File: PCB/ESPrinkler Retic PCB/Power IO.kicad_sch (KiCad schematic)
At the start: 23 parts, among them J1 Conn_01x02, J5 Conn_01x02, J6 Conn_01x02, J7 Conn_01x10, Q2 Q_NMOS, Q3 Q_NMOS, U2 LM2596S-5

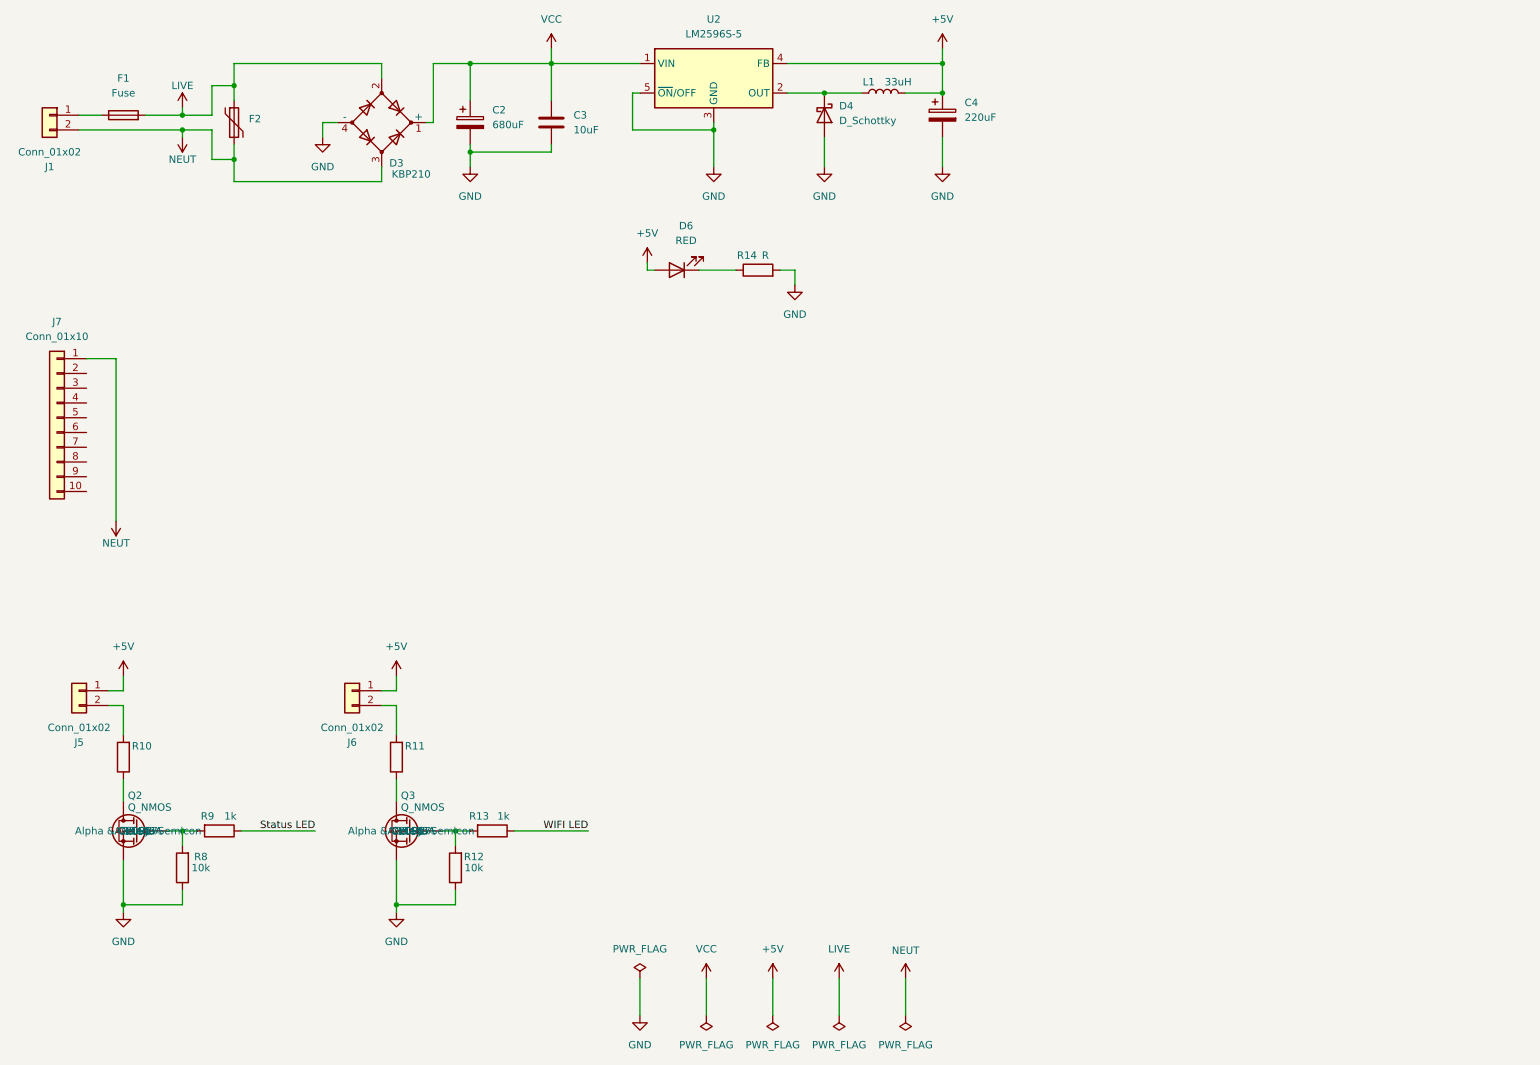
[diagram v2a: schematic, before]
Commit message: Initial schematic design completed
Finish initial schematic design and source all required components. DRC completed with only minor warnings (regarding net names, no worries). Move on to begin PCB design
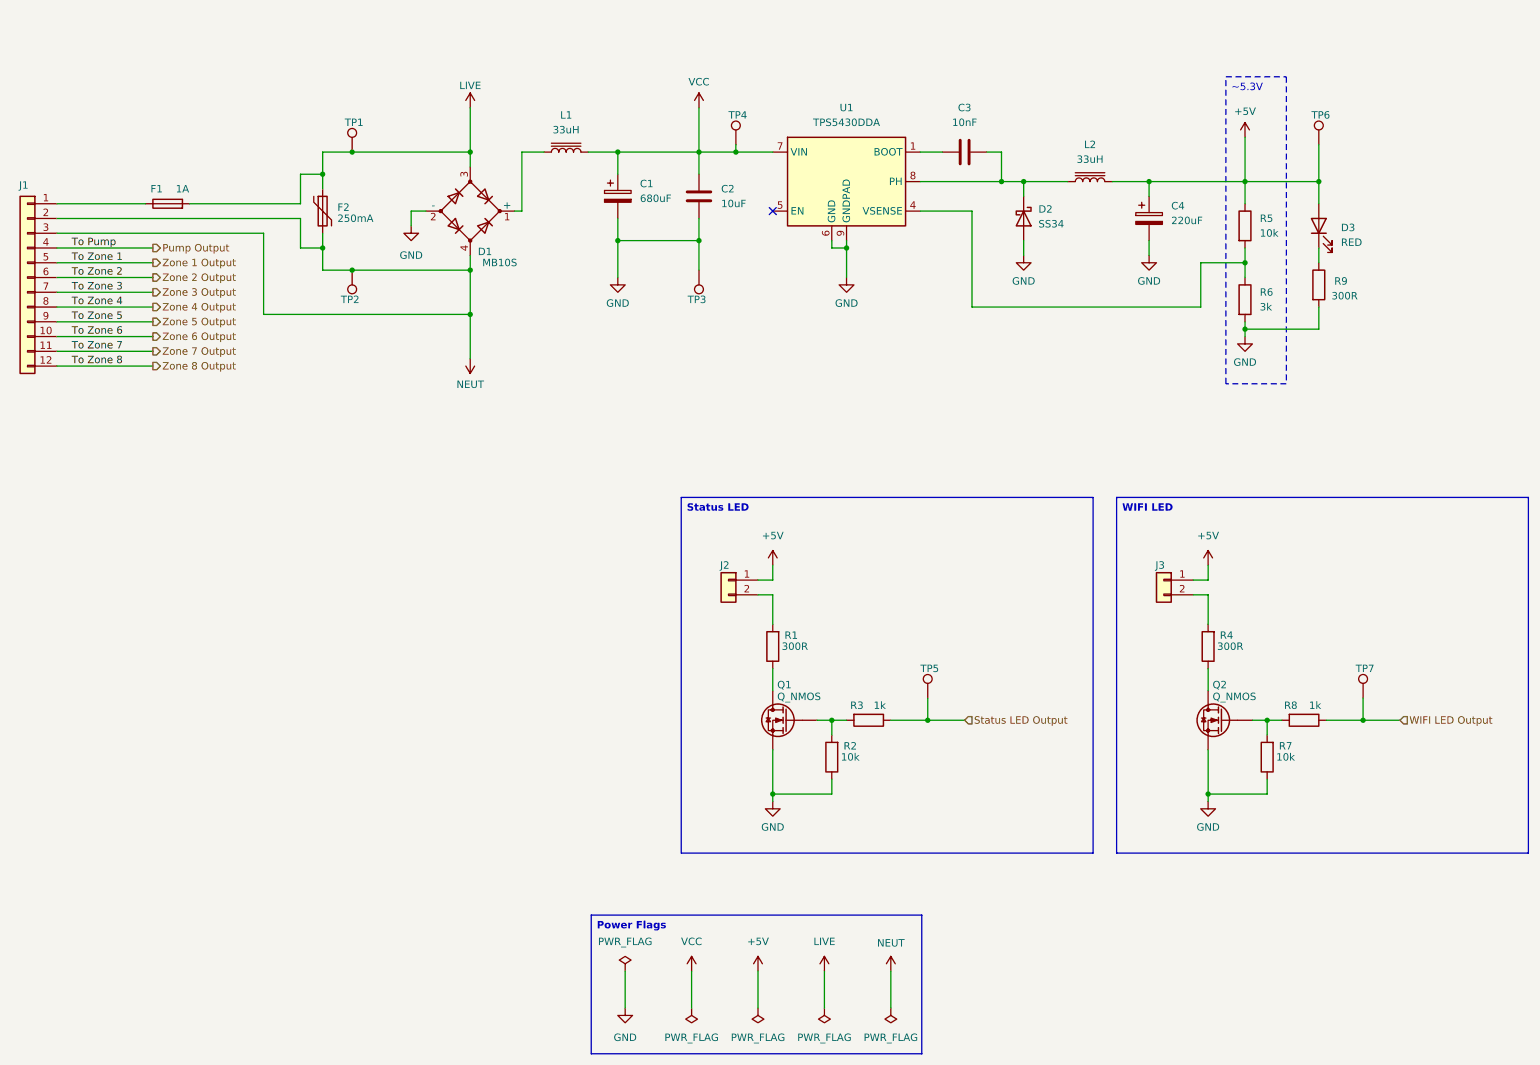
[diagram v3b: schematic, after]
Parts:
- removed J1: Conn_01x02, symbol Connector_Generic:Conn_01x02
- removed J7: Conn_01x10, symbol Connector_Generic:Conn_01x10
- removed L1: 33uH, symbol Device:L
- removed U2: LM2596S-5, Package_TO_SOT_SMD:TO-263-5_TabPin3, symbol Regulator_Switching:LM2596S-5
- added C3: 10nF, Capacitor_SMD:C_0805_2012Metric, symbol Device:C
- added J1: ~, symbol Connector_Generic:Conn_01x12
- added L1, L2: 33uH, Inductor_SMD:L_APV_ANR5045, symbol Device:L_Iron
- added R5: 10k, Resistor_SMD:R_0805_2012Metric, symbol Device:R
- added R6: 3k, Resistor_SMD:R_0805_2012Metric, symbol Device:R
- added TP1, TP2, TP3, TP4, TP5, TP6, TP7: TestPoint, TestPoint:TestPoint_Pad_D1.5mm, symbol Connector:TestPoint
- added U1: TPS5430DDA, Package_SO:TI_SO-PowerPAD-8_ThermalVias, symbol Regulator_Switching:TPS5430DDA
- C1: renamed from C2; footprint (none) -> Capacitor_THT:CP_Radial_D13.0mm_P5.00mm; Manufacturer (none) -> CX(Dongguan Chengxing Elec); Manufacturer P/N (none) -> GR687M050J20RR0VH4FP0; Supplier (none) -> LCSC; Supplier P/N (none) -> C26225
- C2: renamed from C3; footprint (none) -> Capacitor_SMD:C_1206_3216Metric; Manufacturer (none) -> Samsung Electro-Mechanics; Manufacturer P/N (none) -> CL31A106KBHNNNE; Supplier (none) -> LCSC; Supplier P/N (none) -> C13585
- C4: footprint (none) -> Capacitor_THT:CP_Radial_D6.3mm_P2.50mm; Manufacturer (none) -> CX(Dongguan Chengxing Elec); Manufacturer P/N (none) -> GR227M010E11RR0VH4FP0; Supplier (none) -> LCSC; Supplier P/N (none) -> C2036
- D1: renamed from D3; value KBP210 -> MB10S; footprint (none) -> Package_SO:OnSemi_751EP_SOIC-4_3.9x4.725mm_P2.54mm; symbol Device:D_Bridge_+AA- -> Device:D_Bridge_+-AA; Manufacturer (none) -> MDD(Microdiode Semiconductor); Manufacturer P/N (none) -> MB10S-50MIL; Supplier (none) -> LCSC; Supplier P/N (none) -> C2488
- D2: renamed from D4; value D_Schottky -> SS34; footprint (none) -> Diode_SMD:D_SMA; Manufacturer (none) -> MDD(Microdiode Semiconductor); Manufacturer P/N (none) -> SS34; Supplier (none) -> LCSC; Supplier P/N (none) -> C8678
- F1: value Fuse -> 1A; footprint (none) -> Fuse:Fuseholder_Cylinder-5x20mm_Schurter_0031_8201_Horizontal_Open; Manufacturer (none) -> XFCN; Manufacturer P/N (none) -> PTF-15; Supplier (none) -> LCSSC; Supplier P/N (none) -> C842712
- F2: value ~ -> 250mA; footprint (none) -> Fuse:Fuse_BelFuse_0ZRE0100FF_L18.7mm_W5.1mm; Manufacturer (none) -> RUILON(Shenzhen Ruilongyuan Elec); Manufacturer P/N (none) -> RLVR240-025; Supplier (none) -> LCSC; Supplier P/N (none) -> C20871
- J2: renamed from J5; footprint (none) -> TerminalBlock_Phoenix:TerminalBlock_Phoenix_PT-1,5-2-5.0-H_1x02_P5.00mm_Horizontal; Manufacturer (none) -> Ningbo Kangnex Elec; Manufacturer P/N (none) -> WJ300V-5.0-2P; Supplier (none) -> LCSC; Supplier P/N (none) -> C8385
- J3: renamed from J6; footprint (none) -> TerminalBlock_Phoenix:TerminalBlock_Phoenix_PT-1,5-2-5.0-H_1x02_P5.00mm_Horizontal; Manufacturer (none) -> Ningbo Kangnex Elec; Manufacturer P/N (none) -> WJ300V-5.0-2P; Supplier (none) -> LCSC; Supplier P/N (none) -> C8385
- R1: renamed from R10; value ~ -> 300R; footprint (none) -> Resistor_SMD:R_0805_2012Metric; Manufacturer (none) -> UNI-ROYAL(Uniroyal Elec); Manufacturer P/N (none) -> 0805W8F3000T5E; Supplier (none) -> LCSC; Supplier P/N (none) -> C17617
- R4: renamed from R11; value ~ -> 300R; footprint (none) -> Resistor_SMD:R_0805_2012Metric; Manufacturer (none) -> UNI-ROYAL(Uniroyal Elec); Manufacturer P/N (none) -> 0805W8F3000T5E; Supplier (none) -> LCSC; Supplier P/N (none) -> C17617
- R9: renamed from R14; value R -> 300R; footprint (none) -> Resistor_SMD:R_0805_2012Metric; Manufacturer (none) -> UNI-ROYAL(Uniroyal Elec); Manufacturer P/N (none) -> 0805W8F3000T5E; Supplier (none) -> LCSC; Supplier P/N (none) -> C17617
- renumbered D6 to D3, Q2 to Q1, Q3 to Q2, R8 to R2, R9 to R3, R12 to R7, R13 to R8
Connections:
- net +5V: now also L2.2, R5.1, TP6.1
- net GND: now also D1.2 (-), R6.2, TP3.1, U1.6 (GND), U1.9 (GNDPAD); no longer D1.4 (-)
- net LIVE: now also D1.3, TP1.1; no longer D1.2
- net NEUT: now also D1.4, J1.2 (Pin_2), J1.3 (Pin_3), TP2.1; no longer D1.3
- net VCC: now also L1.2, TP4.1, U1.7 (VIN); no longer D1.1 (+)
- net at D2.1 (K): now also C3.2, L2.1, U1.8 (PH)
- net at F1.1: now also J1.1 (Pin_1)
- net Status LED renamed Status LED Output
- net Status LED Output: now also TP5.1
- net WIFI LED renamed WIFI LED Output
- net WIFI LED Output: now also TP7.1
- new net: D1.1 (+), L1.1
- new net: C3.1, U1.1 (BOOT)
- new net: R5.2, R6.1, U1.4 (VSENSE)
- new net Pump Output: J1.4 (Pin_4)
- new net Zone 1 Output: J1.5 (Pin_5)
- new net Zone 2 Output: J1.6 (Pin_6)
- new net Zone 3 Output: J1.7 (Pin_7)
- new net Zone 4 Output: J1.8 (Pin_8)
- new net Zone 5 Output: J1.9 (Pin_9)
- new net Zone 6 Output: J1.10 (Pin_10)
- new net Zone 7 Output: J1.11 (Pin_11)
- new net Zone 8 Output: J1.12 (Pin_12)
- no-connect marks 0 -> 1
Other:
- moved on the sheet: C1, C2, C4, D1, D2, D3, F1, F2, J2, J3, Q1, Q2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

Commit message: Begin work on PCB
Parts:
- J1: footprint (none) -> Footprints:HB9500M-9.5-12P
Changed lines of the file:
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@@
 			)
 		)
-		(property "Footprint" ""
+		(property "Footprint" "Footprints:HB9500M-9.5-12P"
 			(at 20.32 62.23 0)
 			(effects

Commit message: Attempting to source different 12 pin connector
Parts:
- J1: footprint Footprints:HB9500M-9.5-12P -> Connector_Phoenix_SPT:PhoenixContact_SPT_1.5_12-H-3.5_1x12_P3.5mm_Horizontal
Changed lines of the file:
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@@
 			)
 		)
-		(property "Footprint" "Footprints:HB9500M-9.5-12P"
+		(property "Footprint" "Connector_Phoenix_SPT:PhoenixContact_SPT_1.5_12-H-3.5_1x12_P3.5mm_Horizontal"
 			(at 20.32 62.23 0)
 			(effects

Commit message: Found potential solution for main header connector
Choose main header solution, create footprint for header, update SCH and PCB
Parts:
- J1: footprint Connector_Phoenix_SPT:PhoenixContact_SPT_1.5_12-H-3.5_1x12_P3.5mm_Horizontal -> Footprints:DBT30C-7.62-12P-BK-P; Manufacturer Ningbo Kangnex Elec -> DORABO; Manufacturer P/N HB9500M-9.5-12P -> DBT30C-7.62-12P-BK-P; Supplier P/N C601245 -> C395945
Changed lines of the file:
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@@
 			)
 		)
-		(property "Footprint" "Connector_Phoenix_SPT:PhoenixContact_SPT_1.5_12-H-3.5_1x12_P3.5mm_Horizontal"
+		(property "Footprint" "Footprints:DBT30C-7.62-12P-BK-P"
 			(at 20.32 62.23 0)
 			(effects
@@
 			)
 		)
-		(property "Description" "1x12P Corner With Cover Plate 12 1 9.5mm -40℃~+105℃ 32A 750V Black 12~22 Straight Needle 4 Plugin,P=9.5mm Barrier Terminal Blocks ROHS"
+		(property "Description" "1x12P Mid Leg Double-sided 12 1 7.62mm 17.5A -40℃~+105℃ 450V Black 14~22 Straight Needle 1.5 Plugin,P=7.62mm Barrier Terminal Blocks ROHS"
 			(at 20.32 62.23 0)
 			(effects
@@
 			)
 		)
-		(property "Manufacturer" "Ningbo Kangnex Elec"
+		(property "Manufacturer" "DORABO"
 			(at 20.32 62.23 0)
 			(effects
@@
 			)
 		)
-		(property "Manufacturer P/N" "HB9500M-9.5-12P"
+		(property "Manufacturer P/N" "DBT30C-7.62-12P-BK-P"
 			(at 20.32 62.23 0)
 			(effects
@@
 			)
 		)
-		(property "Supplier P/N" "C601245"
+		(property "Supplier P/N" "C395945"
 			(at 20.32 62.23 0)
 			(effects

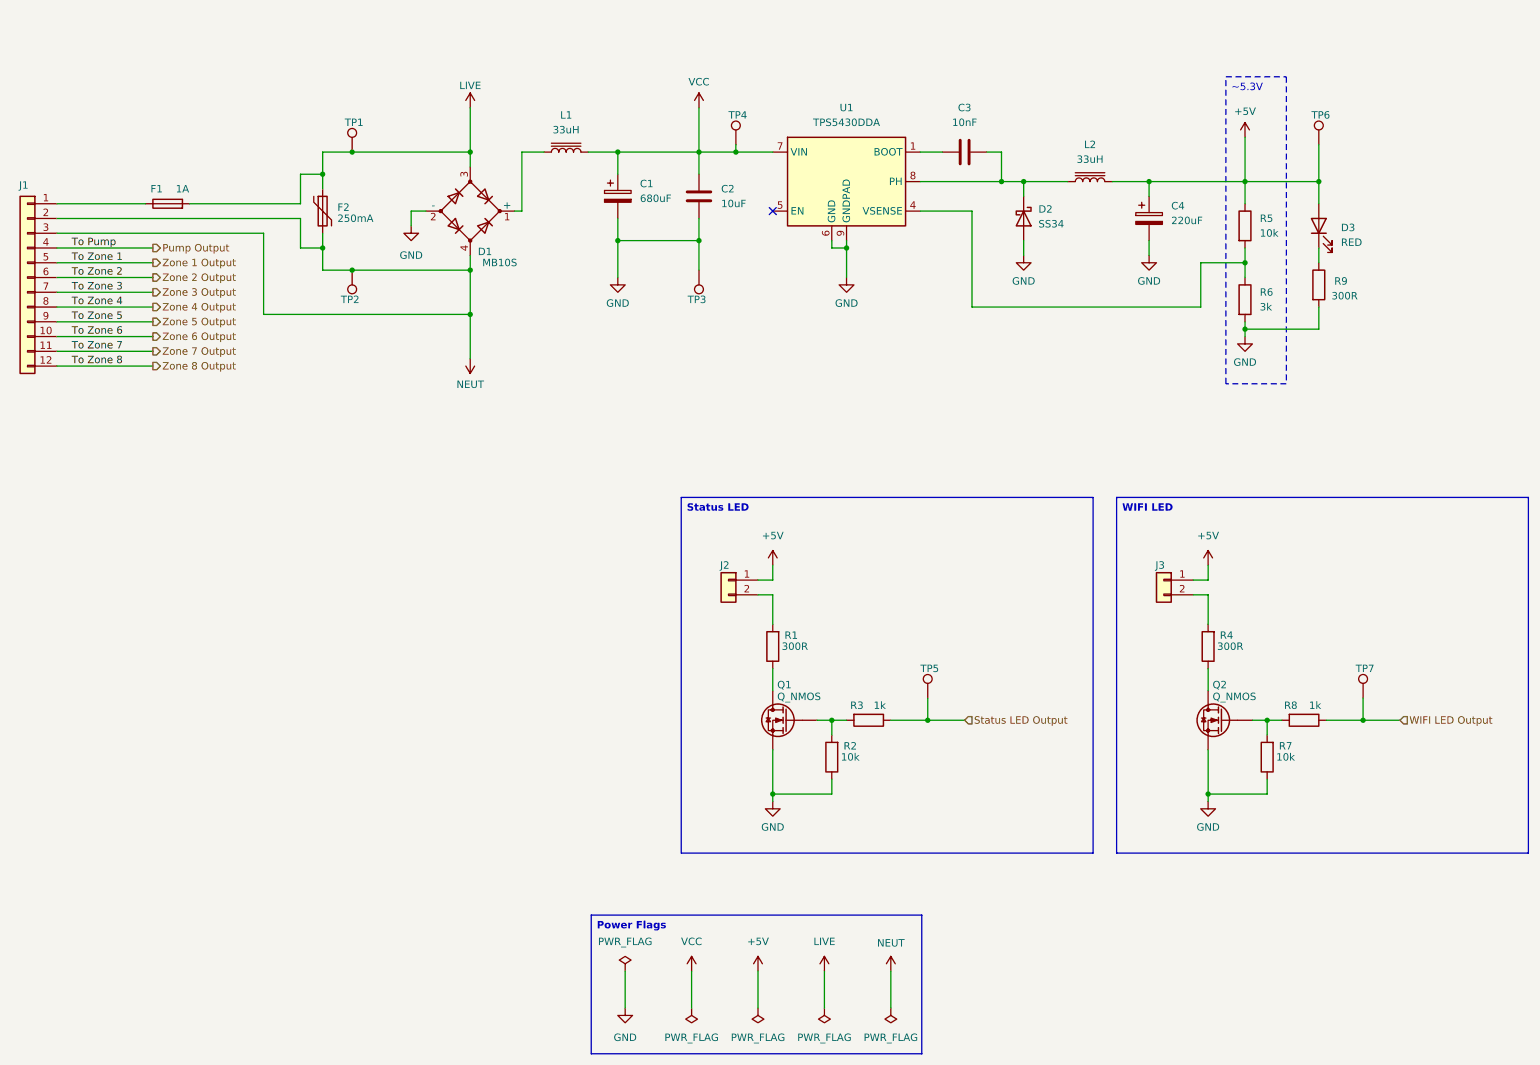
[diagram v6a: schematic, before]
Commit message: PCB and SCH work
Fix symbol issue for mosfet.

Continue PCB design layout
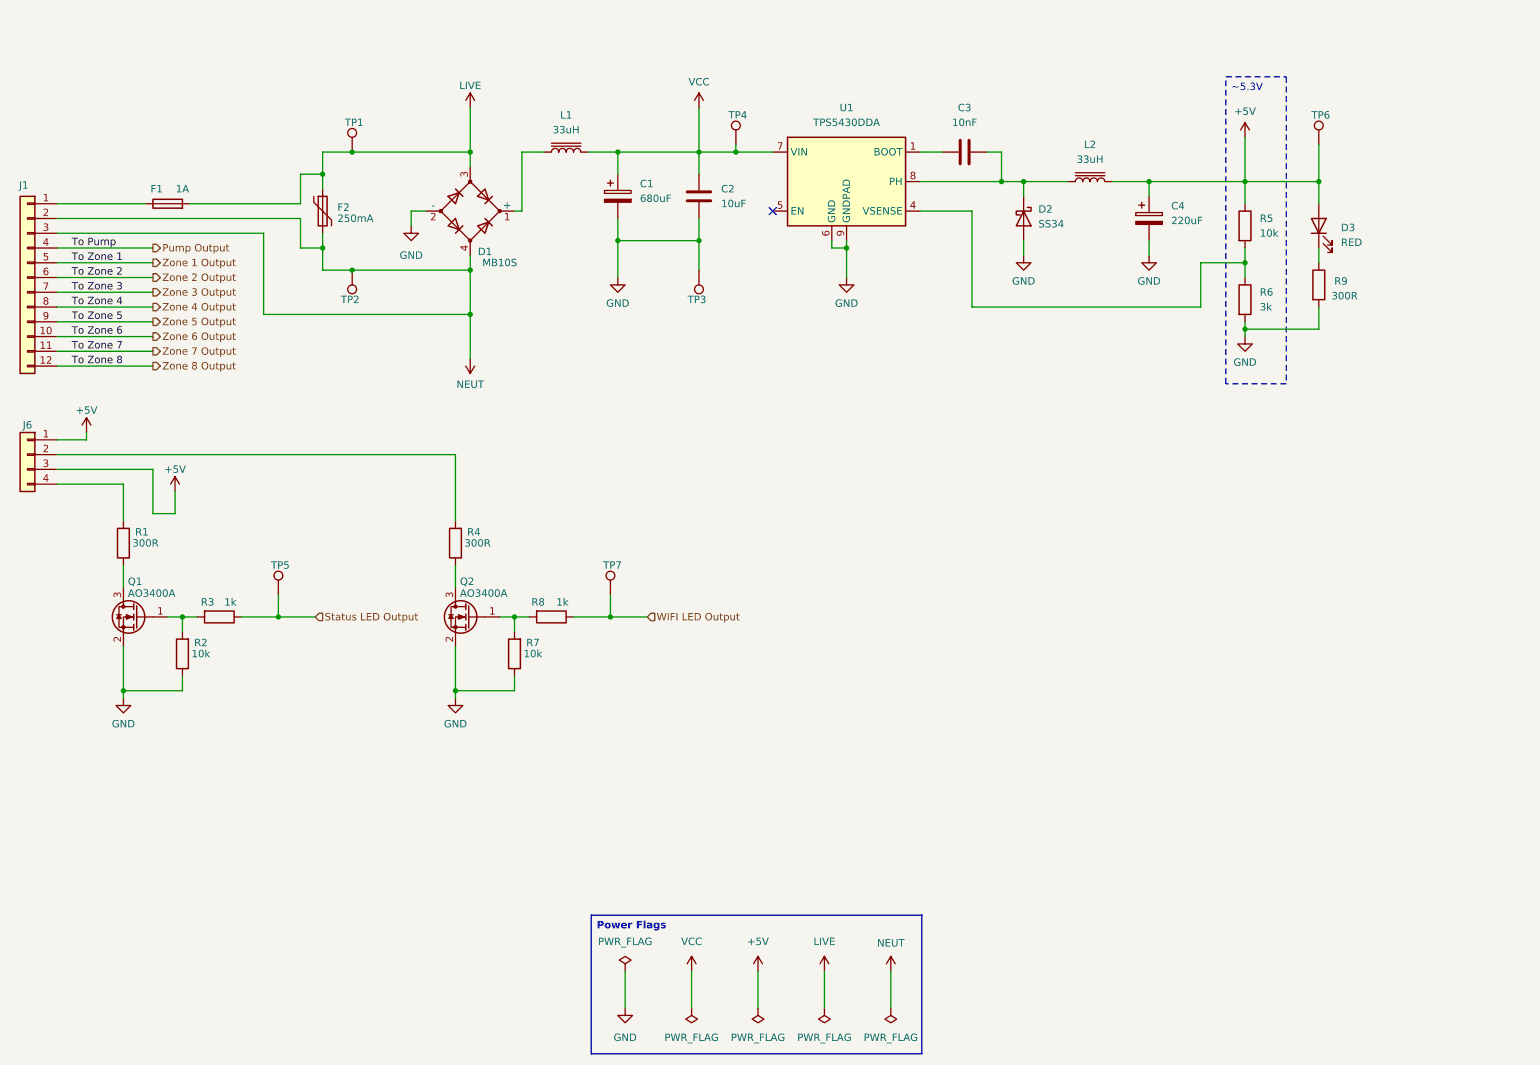
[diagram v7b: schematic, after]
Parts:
- removed J2, J3: Conn_01x02, TerminalBlock_Phoenix:TerminalBlock_Phoenix_PT-1,5-2-5.0-H_1x02_P5.00mm_Horizontal, symbol Connector_Generic:Conn_01x02
- added J6: Conn_01x04, TerminalBlock_Phoenix:TerminalBlock_Phoenix_PT-1,5-4-5.0-H_1x04_P5.00mm_Horizontal, symbol Connector_Generic:Conn_01x04
- Q1, Q2: value Q_NMOS -> AO3400A; symbol Device:Q_NMOS -> Transistor_FET:Q_NMOS_GSD
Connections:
- net +5V: now also J6.1 (Pin_1), J6.3 (Pin_3)
- net GND: now also Q1.2 (S), Q2.2 (S); no longer Q1.S, Q2.S
- net at R2.2, R3.2: now also Q1.1 (G); no longer Q1.G
- net at R7.2, R8.2: now also Q2.1 (G); no longer Q2.G
- net at R1.1: now also Q1.3 (D); no longer Q1.D
- net at R4.1: now also Q2.3 (D); no longer Q2.D
- net at R1.2: now also J6.4 (Pin_4)
- net at R4.2: now also J6.2 (Pin_2)
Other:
- moved on the sheet: R1, R2, R3, R4, R7, R8, TP5, TP7
